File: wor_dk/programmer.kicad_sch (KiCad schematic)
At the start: 41 parts, among them J601 USB_C_Receptacle_USB2.0_14P, J602 Prog, Q601 BSS84, SW601 SW_Push, U601 LPC11U35FHI33_501, U602 TLV1117-33, Y601 Crystal

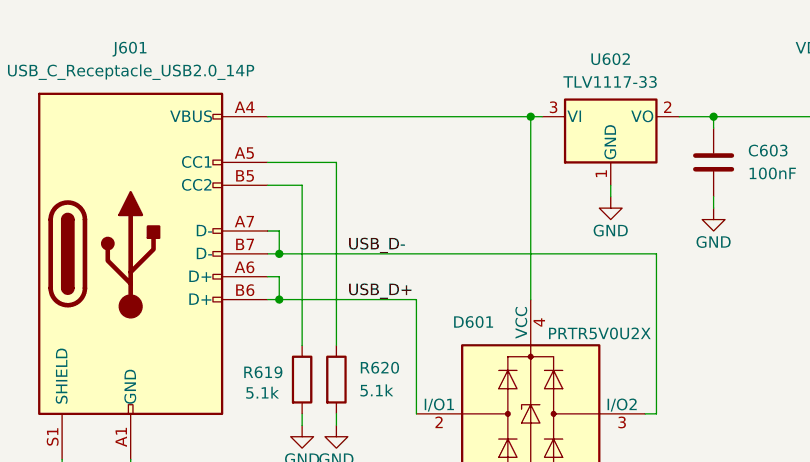
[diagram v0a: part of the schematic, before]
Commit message: wor_dk: add 100 mA fuses for USB power
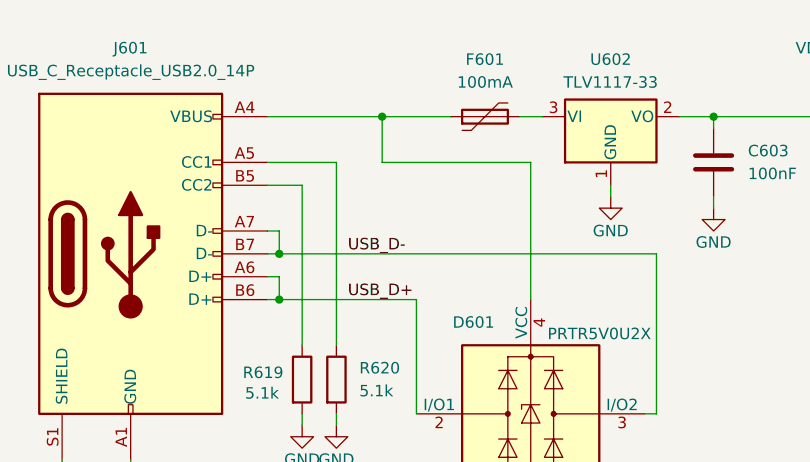
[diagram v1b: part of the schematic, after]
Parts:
- added F601: 100mA, Fuse:Fuse_0603_1608Metric, symbol Device:Polyfuse
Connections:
- net at D601.4 (VCC), J601.A4 (VBUS), J601.A9 (VBUS)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: now also F601.1; no longer U602.3 (VI)
- new net: F601.2, U602.3 (VI)
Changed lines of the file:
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@@
 	)
 	(junction
-		(at 72.39 26.67)
-		(diameter 0)
-		(color 0 0 0 0)
-	)
-	(junction
 		(at 29.21 173.99)
 		(diameter 0)
@@
 	)
 	(junction
+		(at 55.88 26.67)
+		(diameter 0)
+		(color 0 0 0 0)
+	)
+	(junction
 		(at 220.98 92.71)
 		(diameter 0)
@@
 	(wire
 		(pts
-			(xy 43.18 26.67) (xy 72.39 26.67)
-		)
-		(stroke
-			(width 0)
-			(type default)
-		)
-	)
-	(wire
-		(pts
 			(xy 220.98 82.55) (xy 232.41 82.55)
 		)
@@
 	(wire
 		(pts
+			(xy 43.18 26.67) (xy 55.88 26.67)
+		)
+		(stroke
+			(width 0)
+			(type default)
+		)
+	)
+	(wire
+		(pts
 			(xy 44.45 39.37) (xy 43.18 39.37)
 		)
@@
 	(wire
 		(pts
+			(xy 71.12 26.67) (xy 73.66 26.67)
+		)
+		(stroke
+			(width 0)
+			(type default)
+		)
+	)
+	(wire
+		(pts
 			(xy 120.65 172.72) (xy 120.65 173.99)
 		)
@@
 	(wire
 		(pts
+			(xy 72.39 31.75) (xy 55.88 31.75)
+		)
+		(stroke
+			(width 0)
+			(type default)
+		)
+	)
+	(wire
+		(pts
 			(xy 92.71 35.56) (xy 92.71 36.83)
 		)
@@
 	(wire
 		(pts
+			(xy 72.39 46.99) (xy 72.39 31.75)
+		)
+		(stroke
+			(width 0)
+			(type default)
+		)
+	)
+	(wire
+		(pts
 			(xy 226.06 31.75) (xy 241.3 31.75)
 		)
@@
 	(wire
 		(pts
-			(xy 72.39 26.67) (xy 73.66 26.67)
-		)
-		(stroke
-			(width 0)
-			(type default)
-		)
-	)
-	(wire
-		(pts
 			(xy 106.68 27.94) (xy 106.68 26.67)
 		)
@@
 	(wire
 		(pts
+			(xy 55.88 31.75) (xy 55.88 26.67)
+		)
+		(stroke
+			(width 0)
+			(type default)
+		)
+	)
+	(wire
+		(pts
 			(xy 199.39 107.95) (xy 238.76 107.95)
 		)
@@
 	(wire
 		(pts
+			(xy 55.88 26.67) (xy 63.5 26.67)
+		)
+		(stroke
+			(width 0)
+			(type default)
+		)
+	)
+	(wire
+		(pts
 			(xy 220.98 92.71) (xy 220.98 91.44)
 		)
@@
 	(wire
 		(pts
-			(xy 72.39 46.99) (xy 72.39 26.67)
-		)
-		(stroke
-			(width 0)
-			(type default)
-		)
-	)
-	(wire
-		(pts
 			(xy 199.39 146.05) (xy 200.66 146.05)
 		)
@@
 					(unit 1)
 				)
+			)
+		)
+	)
+	(symbol
+		(lib_id "Device:Polyfuse")
+		(at 67.31 26.67 90)
+		(unit 1)
+		(exclude_from_sim no)
+		(in_bom yes)
+		(on_board yes)
+		(dnp no)
+		(fields_autoplaced yes)
+		(property "Reference" "F601"
+			(at 67.31 20.32 90)
+			(effects
+				(font
+					(size 1.27 1.27)
+				)
+			)
+		)
+		(property "Value" "100mA"
+			(at 67.31 22.86 90)
+			(effects
+				(font
+					(size 1.27 1.27)
+				)
+			)
+		)
+		(property "Footprint" "Fuse:Fuse_0603_1608Metric"
+			(at 72.39 25.4 0)
+			(effects
+				(font
+					(size 1.27 1.27)
+				)
+				(justify left)
+				(hide yes)
+			)
+		)
+		(property "Datasheet" "https://datasheet.lcsc.com/lcsc/1809211423_TECHFUSE-SMD0603-010_C70047.pdf"
+			(at 67.31 26.67 0)
+			(effects
+				(font
+					(size 1.27 1.27)
+				)
+				(hide yes)
+			)
+		)
+		(property "Description" "15V 100mA 40A 300mA 0603"
+			(at 67.31 26.67 0)
+			(effects
+				(font
+					(size 1.27 1.27)
+				)
+				(hide yes)
+			)
+		)
+		(property "LCSC" "C70047"
+			(at 67.31 26.67 0)
+			(effects
+				(font
+					(size 1.27 1.27)
+				)
+				(hide yes)
+			)
+		)
+		(property "Manufacturer" "TECHFUSE"
+			(at 67.31 26.67 0)
+			(effects
+				(font
+					(size 1.27 1.27)
+				)
+				(hide yes)
+			)
+		)
+		(property "Part Number" "SMD0603-010"
+			(at 67.31 26.67 0)
+			(effects
+				(font
+					(size 1.27 1.27)
+				)
+				(hide yes)
+			)
+		)
+		(property "Comment" "100mA is max we are allowed to draw without negatiation; host side should also have a fuse (at higher current)."
+			(at 67.31 26.67 0)
+			(effects
+				(font
+					(size 1.27 1.27)
+				)
+				(hide yes)
+			)
+		)
+		(pin "1"
+		)
+		(pin "2"
+		)
+		(instances
+			(project "wor_dk"
+				(path "/8d3147eb-060b-4f65-bf42-ed06a58b21ba/8ac0f979-ce0c-42a5-9e8d-dda3e347b4b7"
+					(reference "F601")
+					(unit 1)
+				)

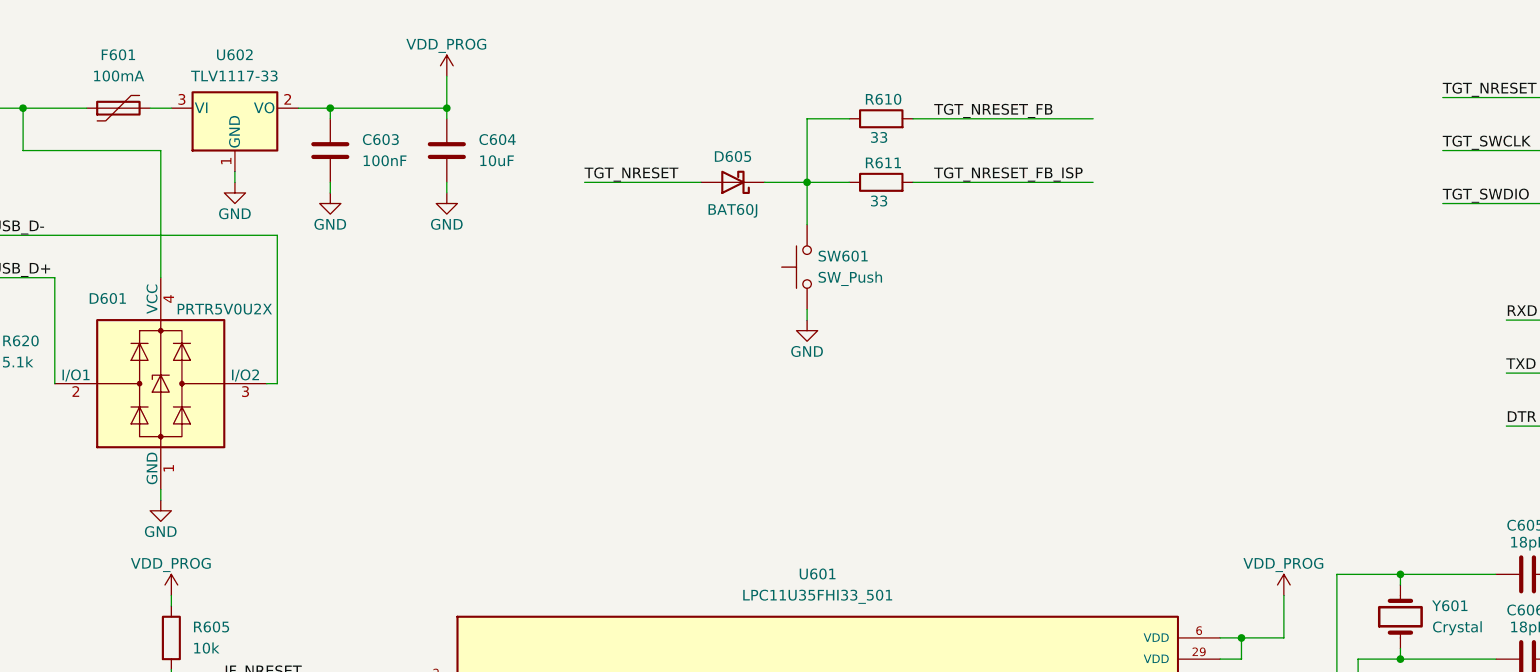
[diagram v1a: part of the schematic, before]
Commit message: wor_dk: add capacitor + ferrite for LPC11U35 USB
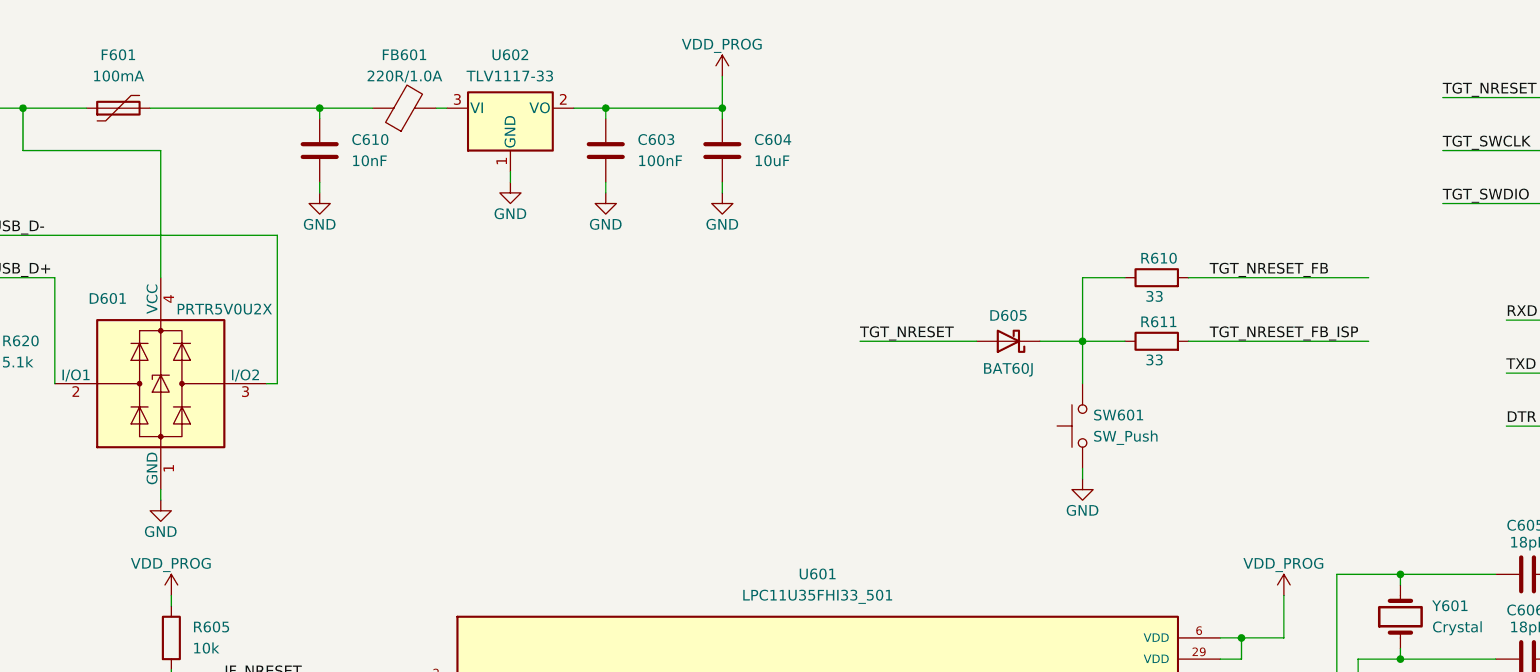
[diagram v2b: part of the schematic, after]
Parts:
- added C610: 10nF, Capacitor_SMD:C_0201_0603Metric, symbol Device:C
- added FB601: 220R/1.0A, Resistor_SMD:R_0402_1005Metric, symbol Device:FerriteBead
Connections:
- net GND: now also C610.2
- net at U602.3 (VI): now also FB601.2; no longer F601.2
- new net: C610.1, F601.2, FB601.1
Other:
- moved on the sheet: C603, C604, D605, R610, R611, SW601, U602

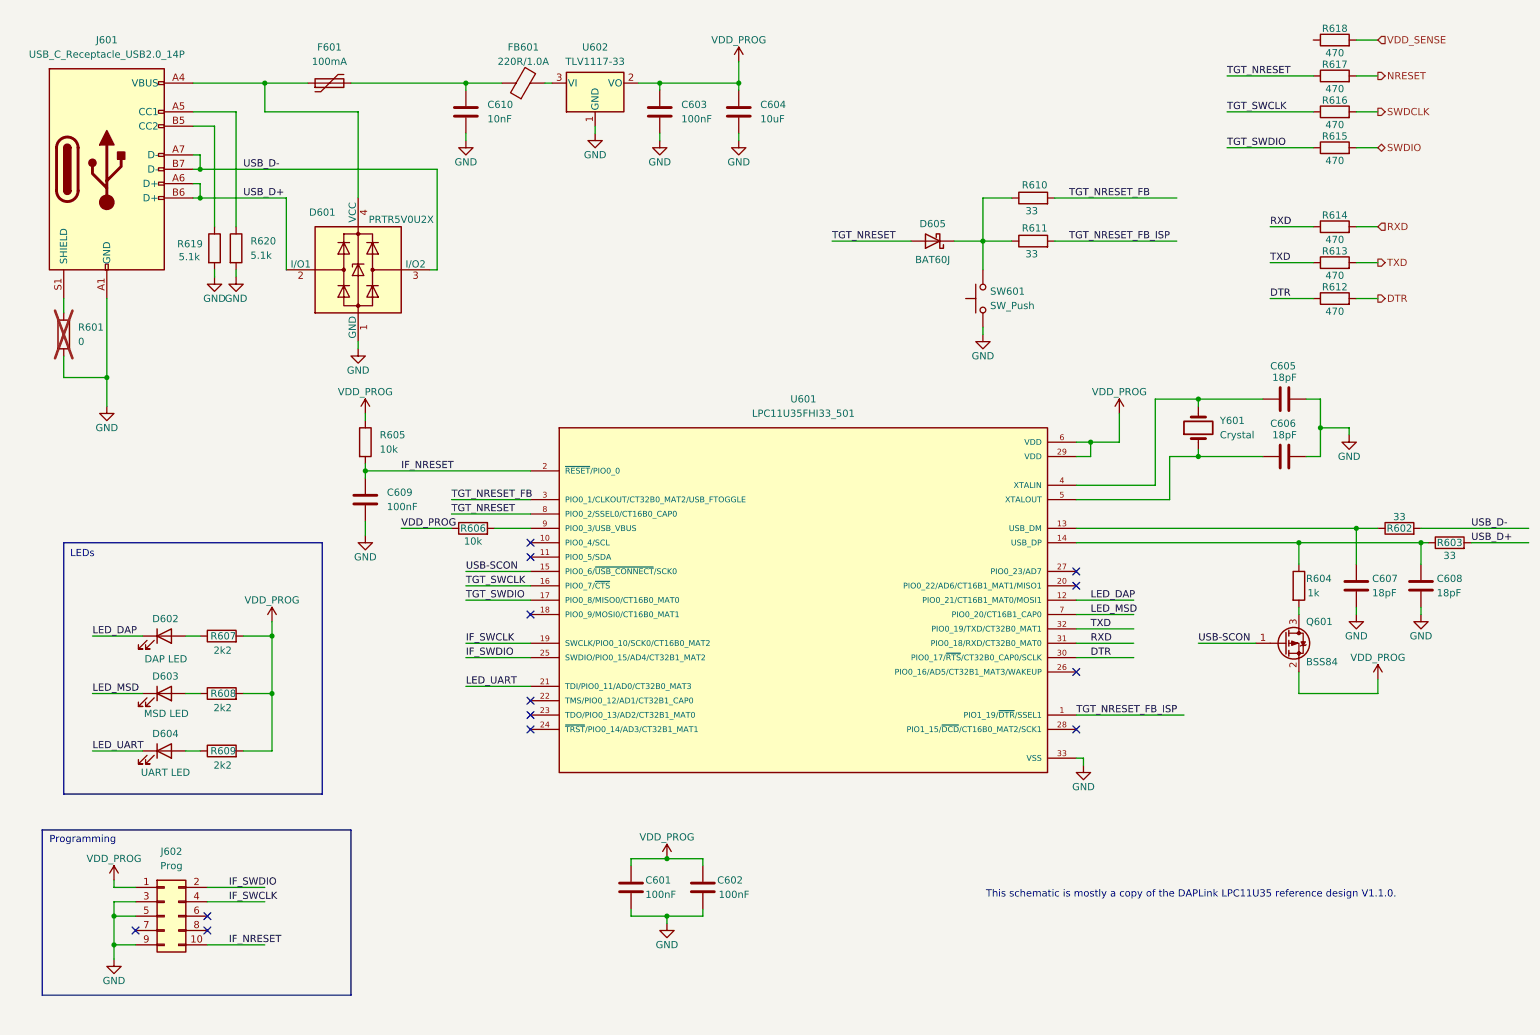
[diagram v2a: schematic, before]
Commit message: wor_dk: remove VDD sense pin, add external SWD header
VDD sense is not useful since we do not support VDD level sensing and
the target voltage is always 3.3V.

The external SWD header allows using the board to program a third
party board (requires disconnecting the DUT first).
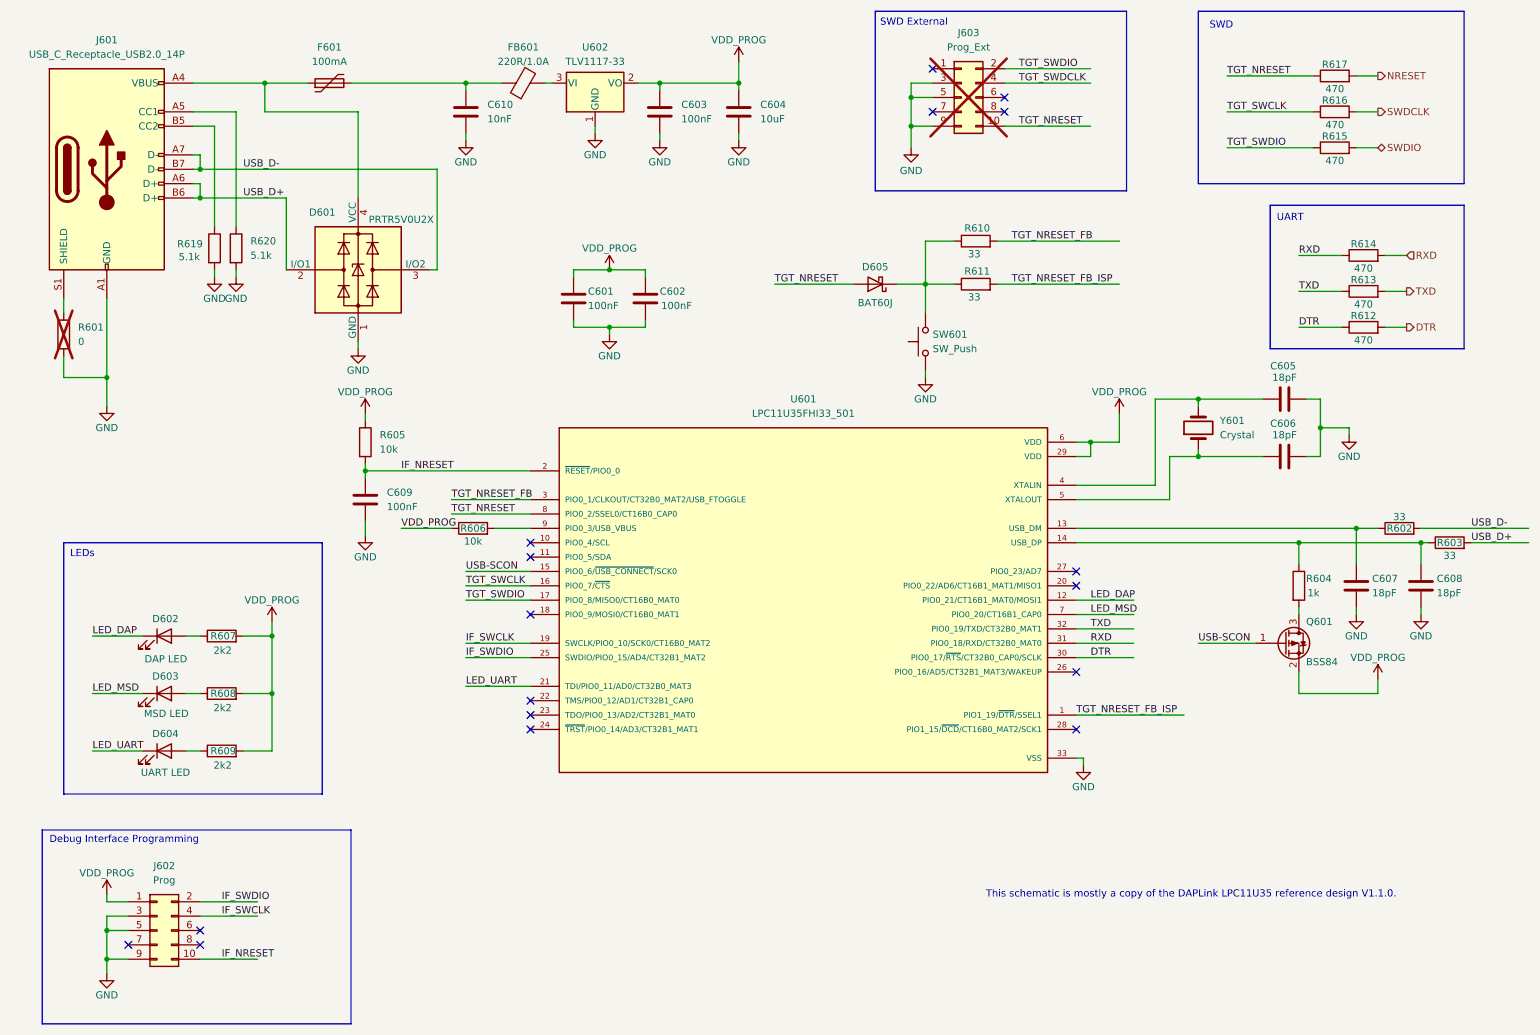
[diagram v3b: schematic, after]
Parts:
- removed R618: 470, symbol Device:R
- added J603: Prog_Ext, Connector_PinHeader_1.27mm:PinHeader_2x05_P1.27mm_Vertical_SMD, symbol Connector_Generic:Conn_02x05_Odd_Even
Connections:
- net GND: now also J603.3 (Pin_3), J603.5 (Pin_5), J603.9 (Pin_9)
- net TGT_NRESET: now also J603.10 (Pin_10)
- net TGT_SWDIO: now also J603.2 (Pin_2)
- new net TGT_SWDCLK: J603.4 (Pin_4)
- no-connect marks 13 -> 17
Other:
- note added: "Debug Interface Programming"
- note added: "SWD"
- note added: "SWD External"
- note added: "UART"
- note removed: "Programming"
- moved on the sheet: C601, C602, D605, J602, R610, R611, R612, R613, R614, SW601

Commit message: wor_dk: remove controller & re-annotate schematics
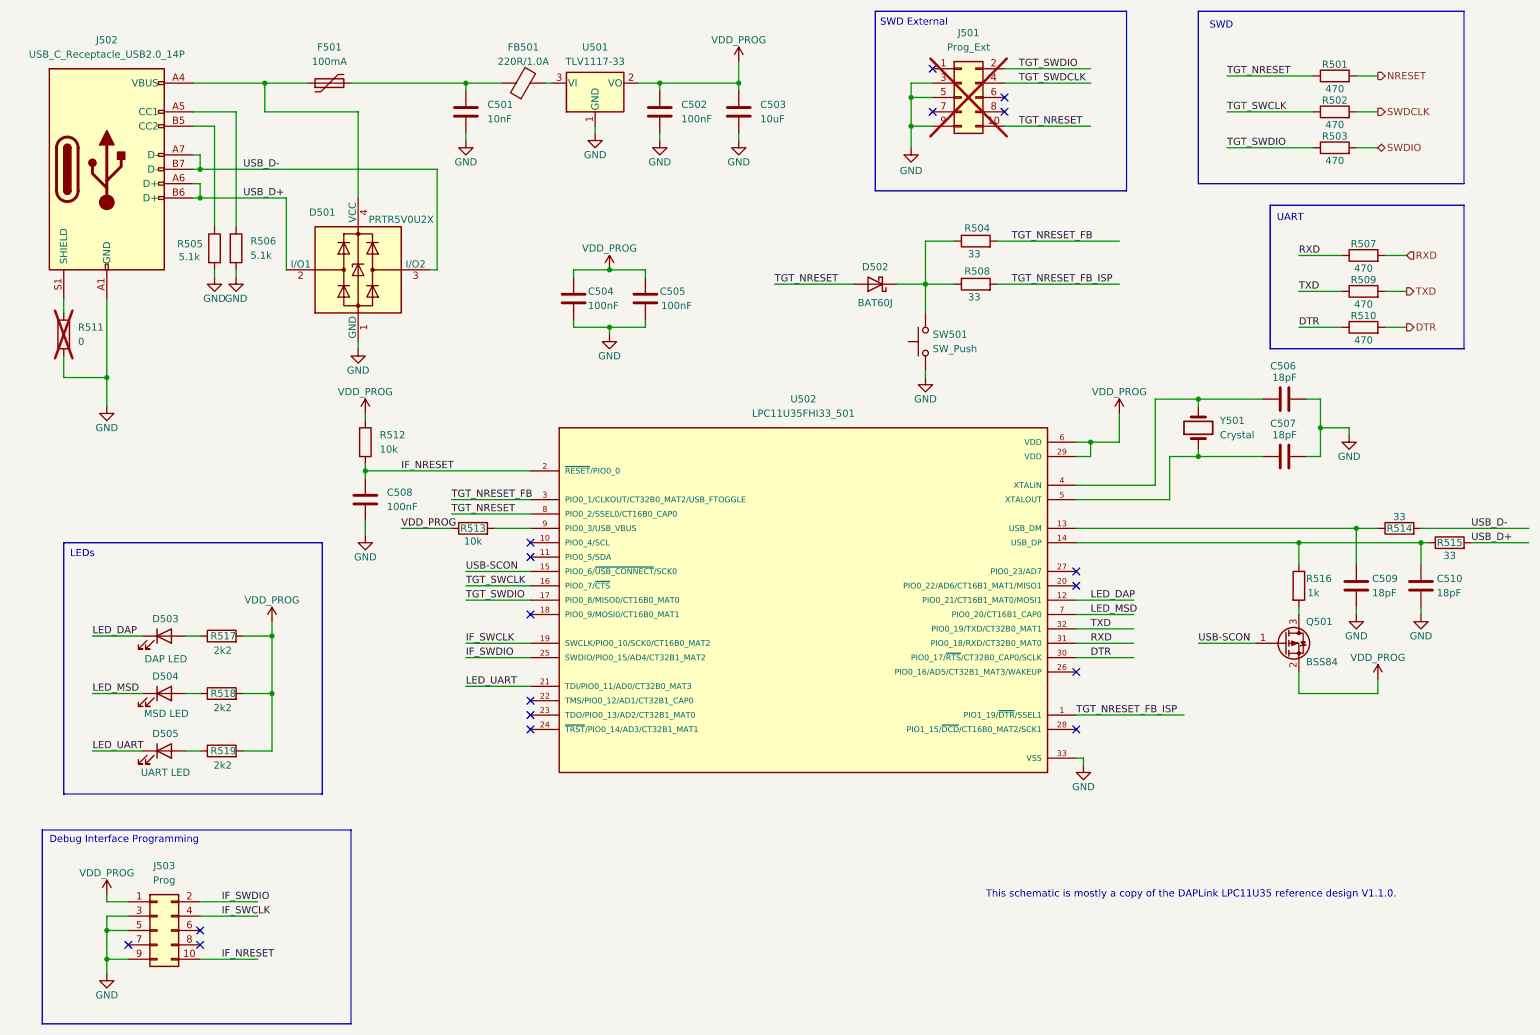
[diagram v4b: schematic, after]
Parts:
- renumbered C610 to C501, C603 to C502, C604 to C503, C601 to C504, C602 to C505, C605 to C506, C606 to C507, C609 to C508, C607 to C509, C608 to C510, D601 to D501, D605 to D502, D602 to D503, D603 to D504, D604 to D505, F601 to F501, FB601 to FB501, J603 to J501, J601 to J502, J602 to J503, Q601 to Q501, R617 to R501, R616 to R502, R615 to R503, R610 to R504, R619 to R505, R620 to R506, R614 to R507, R611 to R508, R613 to R509, R612 to R510, R601 to R511, R605 to R512, R606 to R513, R602 to R514, R603 to R515, R604 to R516, R607 to R517, R608 to R518, R609 to R519, SW601 to SW501, U602 to U501, U601 to U502, Y601 to Y501
